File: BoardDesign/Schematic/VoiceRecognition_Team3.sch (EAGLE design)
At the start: 52 parts, among them J1 5.5x2.1mm Barrel, Q1 16MHz, X1 USB-A

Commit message: Added Updated Board and BOM, note this will not be the final revision
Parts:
- removed C6: 100nF, rcl:C-USC1206
- removed C7: 10uF, rcl:C-USC1206
- removed LED_GRN, LED_RED, LED_YLW, PWR-BLU: (no value), led:LEDSMT1206
- removed MIC_ON: (no value), adafruit:SWITCH_PUSHBUTTONC&K_KSS
- added LEDARRAY: (no value), adafruit:PINHD-1X8BIG
- added LOCK_RESET: (no value), adafruit:PINHD-1X3
- renumbered JP1 to ICSP_INPUT, JP2 to MIC_INPUT, JP3 to SERVO_OUT
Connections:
- net N$13 renamed MOSI
- net N$17 renamed MISO
- net N$2 renamed SCK
- removed net N$15: C7.1, MIC_INPUT.2, MIC_ON.P$2, VCC_TO_MIC.TP
- removed net N$8: LED_RED.C, R3.2
- removed net SERVO_POS: J1.PWR, SERVO_OUT.1, V_BARREL.TP
- new net LOCK_RESET: LOCK_RESET.2, U$1.PB7(OC0A/OC1C/RTS)
- new net N$2: USB_TO_GND.TP, X1.GND
- new net N$4: LEDARRAY.1, R6.1
- net FUNC_GRN: now also LEDARRAY.3, R7.1, R7.2; no longer LED_GRN.A
- net GND: now also LEDARRAY.2, LEDARRAY.4, LEDARRAY.6, LEDARRAY.8, LOCK_RESET.1; no longer C6.2, C7.2, R3.1, R5.1, R6.1, R7.1, USB_TO_GND.TP, X1.GND
- net N$5: now also LEDARRAY.5, R5.2; no longer PWR-BLU.C, R6.2
- net N$6: now also LEDARRAY.7, NOFUNC_RED.TP, R3.2; no longer LED_GRN.C, R7.2
- net N$7: now also VCC_TO_USB.TP, X1.VBUS; no longer LED_YLW.C, R5.2
- net NOFUNC_RED: now also R3.1; no longer LED_RED.A, NOFUNC_RED.TP
- net VCC: now also J1.PWR, MIC_INPUT.2, R6.2, SERVO_OUT.1, VCC_TO_MIC.TP, V_BARREL.TP; no longer C6.1, MIC_ON.P$1, PWR-BLU.A, VCC_TO_USB.TP, X1.VBUS
- net WARN_YELL: now also R5.1; no longer LED_YLW.A
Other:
- note added: "NC"
- note added: "Tactile Inputs"
- note removed: "PWR_BLU"
- note removed: "Reset Button"
- note removed: "WARN_YELL"
- moved on the sheet: FUNC_GRN, NOFUNC_RED, PWR_BLU, R3, R5, R6, R7, VCC_TO_MIC, WARN_YELL

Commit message: Added a few changes to the board per andrew's suggestion
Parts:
- added C10, C11, C6, C7, C9: 100nF, rcl:C-USC1206
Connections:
- net GND: now also C10.2, C11.2, C6.2, C7.2, C9.2
- net VCC: now also C10.1, C11.1, C6.1, C7.1, C9.1
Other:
- moved on the sheet: C1, C12, C2, Q1

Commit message: Added a connection to ground in the USB jack
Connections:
- removed net N$2: USB_TO_GND.TP, X1.GND
- net GND: now also USB_TO_GND.TP, X1.GND
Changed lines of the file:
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@@
 <part name="GND17" library="supply1" library_urn="urn:adsk.eagle:library:371" deviceset="GND" device=""/>
 <part name="GND21" library="supply1" library_urn="urn:adsk.eagle:library:371" deviceset="GND" device=""/>
+<part name="GND22" library="supply1" library_urn="urn:adsk.eagle:library:371" deviceset="GND" device=""/>
 </parts>
 <sheets>
@@
 <attribute name="VALUE" x="124.46" y="88.9" size="1.778" layer="96" rot="R270"/>
 </instance>
+<instance part="GND22" gate="1" x="33.02" y="88.9" smashed="yes">
+<attribute name="VALUE" x="30.48" y="86.36" size="1.778" layer="96"/>
+</instance>
 </instances>
 <busses>
@@
 <pinref part="C11" gate="G$1" pin="2"/>
 <pinref part="GND21" gate="1" pin="GND"/>
+</segment>
+<segment>
+<pinref part="X1" gate="G$1" pin="GND"/>
+<wire x1="33.02" y1="101.6" x2="33.02" y2="93.98" width="0.1524" layer="91"/>
+<pinref part="USB_TO_GND" gate="G$1" pin="TP"/>
+<pinref part="GND22" gate="1" pin="GND"/>
+<wire x1="33.02" y1="91.44" x2="33.02" y2="93.98" width="0.1524" layer="91"/>
+<junction x="33.02" y="93.98"/>
 </segment>
 </net>
@@
 </segment>
 </net>
-<net name="N$2" class="0">
-<segment>
-<pinref part="X1" gate="G$1" pin="GND"/>
-<wire x1="33.02" y1="101.6" x2="33.02" y2="93.98" width="0.1524" layer="91"/>
-<pinref part="USB_TO_GND" gate="G$1" pin="TP"/>
-</segment>
-</net>

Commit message: yeah
* rearranged bypass caps to VCC

* Added tolerances to bottom right of schem
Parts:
- renumbered VCC_TO_USB to TP_USB
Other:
- note added: "R1, R2, R3, R5, R6, R7: 250mW, 1% TOL"
- note removed: "250mW TOL: 1%"
- moved on the sheet: C10, C11, C12, C2, C6, C7, C9

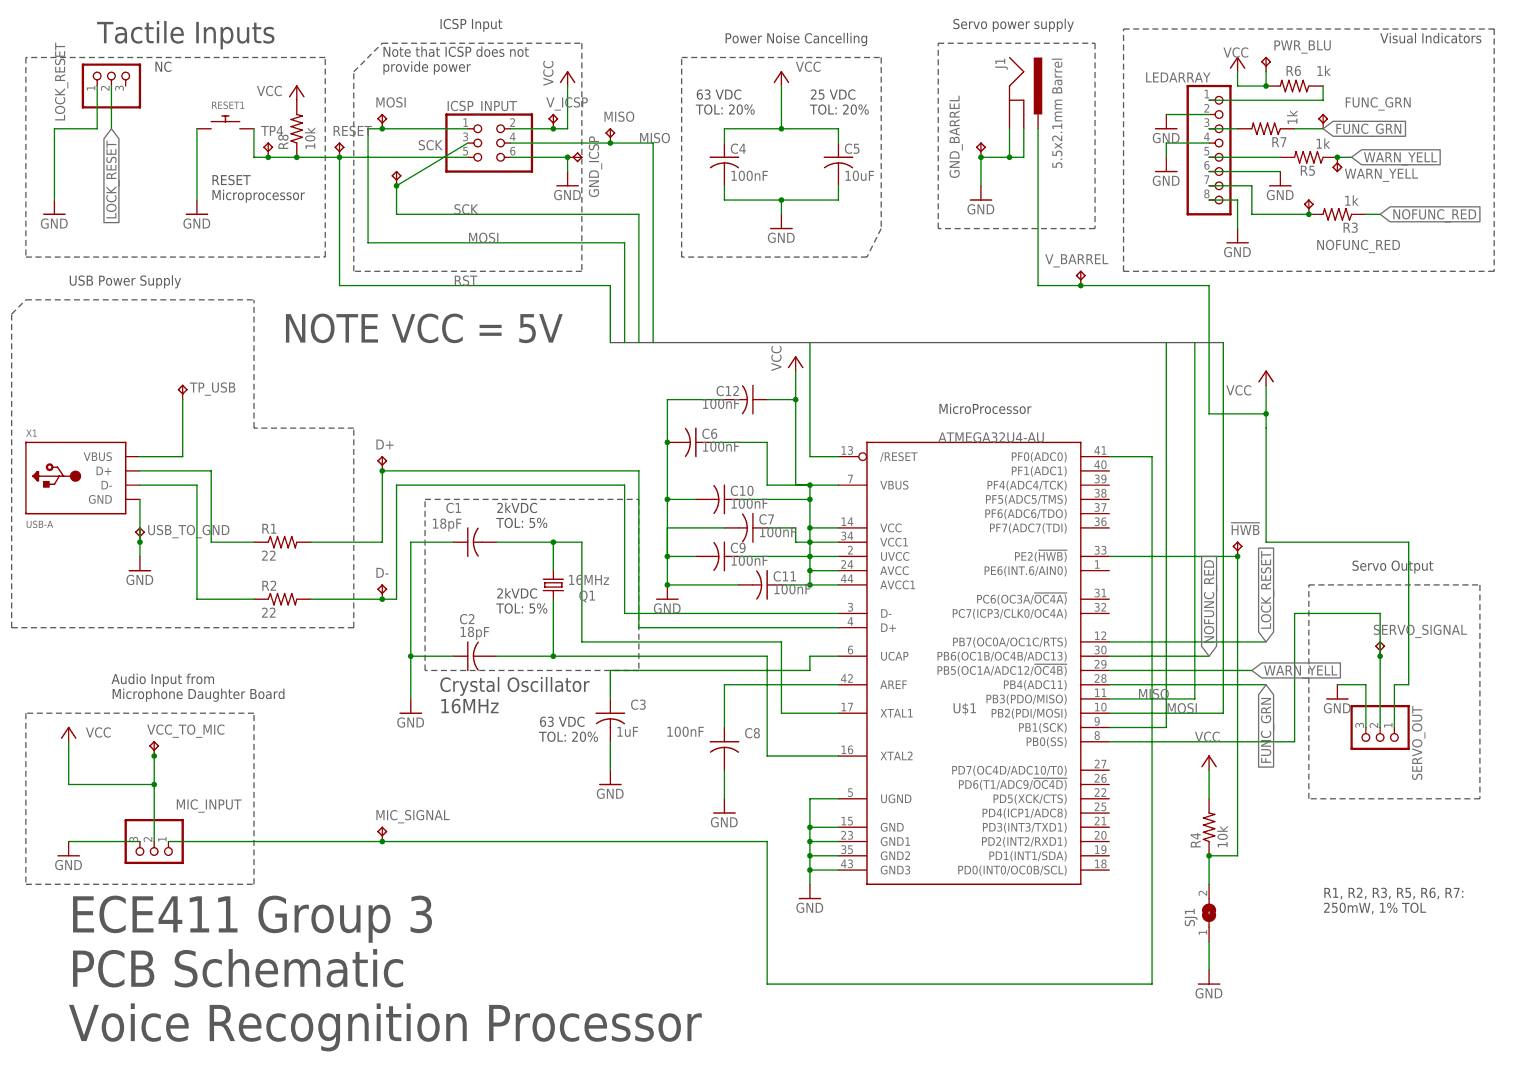
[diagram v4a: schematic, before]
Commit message: VCC caps + cosmetics
* Moved vcc bias caps onto board.
* Moved component names/values around for legibility.
* Rerouted some wires for cosmetic purposes.
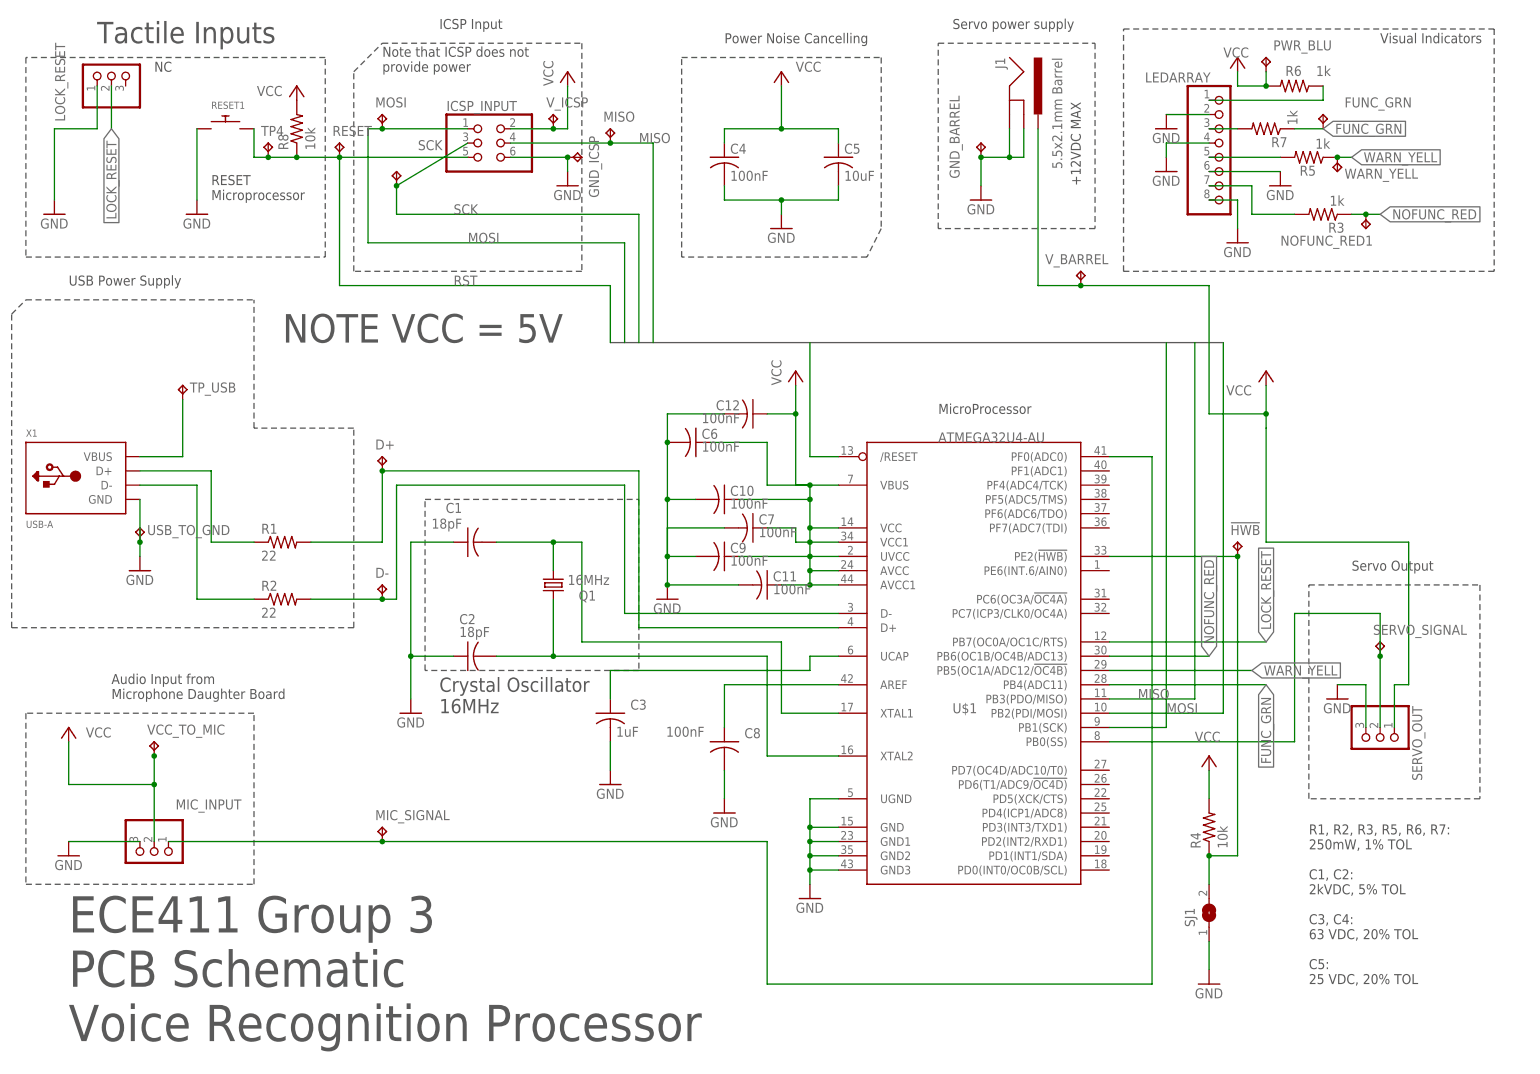
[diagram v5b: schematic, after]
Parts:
- removed NOFUNC_RED: TPTP15SQ, testpad:TPTP15SQ
- added NOFUNC_RED1: TPTP15SQ, testpad:TPTP15SQ
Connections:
- net N$6: no longer NOFUNC_RED.TP
- net NOFUNC_RED: now also NOFUNC_RED1.TP
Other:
- note added: "+12VDC MAX"
- note added: "R1, R2, R3, R5, R6, R7: 250mW, 1% TOL C1, C2: 2kVDC, 5% TOL C3, C4: 63 VDC, 20% TOL C5: 25 VDC, 20% TOL"
- note removed: "25 VDC TOL: 20%"
- note removed: "2kVDC TOL: 5%"
- note removed: "63 VDC TOL: 20%"
- note removed: "R1, R2, R3, R5, R6, R7: 250mW, 1% TOL"
- moved on the sheet: C12, R3
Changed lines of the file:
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@@
 </variantdefs>
 <classes>
-<class number="0" name="default" width="0" drill="0">
+<class number="0" name="VCC" width="0.05" drill="0">
+</class>
+<class number="1" name="GND" width="0.00126875" drill="0">
 </class>
 </classes>
@@
 <part name="FUNC_GRN" library="testpad" library_urn="urn:adsk.eagle:library:385" deviceset="TP" device="TP15SQ" package3d_urn="urn:adsk.eagle:package:27975/1"/>
 <part name="WARN_YELL" library="testpad" library_urn="urn:adsk.eagle:library:385" deviceset="TP" device="TP15SQ" package3d_urn="urn:adsk.eagle:package:27975/1"/>
-<part name="NOFUNC_RED" library="testpad" library_urn="urn:adsk.eagle:library:385" deviceset="TP" device="TP15SQ" package3d_urn="urn:adsk.eagle:package:27975/1"/>
 <part name="!HWB" library="testpad" library_urn="urn:adsk.eagle:library:385" deviceset="TP" device="TP15SQ" package3d_urn="urn:adsk.eagle:package:27975/1"/>
 <part name="RESET" library="testpad" library_urn="urn:adsk.eagle:library:385" deviceset="TP" device="TP15SQ" package3d_urn="urn:adsk.eagle:package:27975/1"/>
@@
 <part name="GND21" library="supply1" library_urn="urn:adsk.eagle:library:371" deviceset="GND" device=""/>
 <part name="GND22" library="supply1" library_urn="urn:adsk.eagle:library:371" deviceset="GND" device=""/>
+<part name="NOFUNC_RED1" library="testpad" library_urn="urn:adsk.eagle:library:385" deviceset="TP" device="TP15SQ" package3d_urn="urn:adsk.eagle:package:27975/1"/>
 </parts>
 <sheets>
@@
 <wire x1="241.3" y1="48.26" x2="241.3" y2="86.36" width="0.1524" layer="97" style="shortdash"/>
 <text x="248.92" y="88.9" size="1.778" layer="97">Servo Output</text>
-<text x="132.08" y="170.18" size="1.778" layer="97">63 VDC
-TOL: 20%</text>
-<text x="152.4" y="170.18" size="1.778" layer="97">25 VDC
-TOL: 20%</text>
-<text x="104.14" y="58.42" size="1.778" layer="97">63 VDC
-TOL: 20%</text>
-<text x="96.52" y="81.28" size="1.778" layer="97">2kVDC
-TOL: 5%</text>
-<text x="96.52" y="96.52" size="1.778" layer="97">2kVDC
-TOL: 5%</text>
 <text x="76.2" y="177.8" size="1.778" layer="97">Note that ICSP does not
 provide power</text>
@@
 <wire x1="208.28" y1="142.24" x2="208.28" y2="185.42" width="0.1524" layer="97" style="shortdash"/>
 <text x="35.56" y="177.8" size="1.778" layer="97">NC</text>
-<text x="243.84" y="27.94" size="1.778" layer="97">R1, R2, R3, R5, R6, R7:
-250mW, 1% TOL</text>
+<text x="241.3" y="15.24" size="1.778" layer="97">R1, R2, R3, R5, R6, R7:
+250mW, 1% TOL
+C1, C2:
+2kVDC, 5% TOL
+C3, C4:
+63 VDC, 20% TOL
+C5:
+25 VDC, 20% TOL</text>
+<text x="200.66" y="157.48" size="1.778" layer="97" rot="R90">+12VDC MAX</text>
 </plain>
 <instances>
@@
 <attribute name="VALUE" x="54.61" y="80.518" size="1.778" layer="96"/>
 </instance>
-<instance part="R3" gate="G$1" x="246.38" y="152.4" rot="R180">
-<attribute name="NAME" x="250.19" y="150.9014" size="1.778" layer="95" rot="R180"/>
-<attribute name="VALUE" x="250.19" y="155.702" size="1.778" layer="96" rot="R180"/>
+<instance part="R3" gate="G$1" x="243.84" y="152.4" rot="R180">
+<attribute name="NAME" x="247.65" y="150.9014" size="1.778" layer="95" rot="R180"/>
+<attribute name="VALUE" x="247.65" y="155.702" size="1.778" layer="96" rot="R180"/>
 </instance>
 <instance part="R4" gate="G$1" x="223.52" y="43.18" rot="R90">
@@
 <attribute name="VALUE" x="226.06" y="180.34" size="1.778" layer="96"/>
 </instance>
-<instance part="P+12" gate="VCC" x="149.86" y="127">
-<attribute name="VALUE" x="147.32" y="124.46" size="1.778" layer="96" rot="R90"/>
+<instance part="P+12" gate="VCC" x="149.86" y="124.46">
+<attribute name="VALUE" x="147.32" y="121.92" size="1.778" layer="96" rot="R90"/>
 </instance>
 <instance part="P+13" gate="VCC" x="223.52" y="55.88">
@@
 <attribute name="VALUE" x="58.42" y="175.26" size="1.778" layer="96" rot="R180"/>
 </instance>
-<instance part="C12" gate="G$1" x="142.24" y="119.38" rot="R270">
-<attribute name="NAME" x="135.636" y="120.015" size="1.778" layer="95"/>
-<attribute name="VALUE" x="133.096" y="117.729" size="1.778" layer="96"/>
+<instance part="C12" gate="G$1" x="142.24" y="116.84" rot="R270">
+<attribute name="NAME" x="135.636" y="117.475" size="1.778" layer="95"/>
+<attribute name="VALUE" x="133.096" y="115.189" size="1.778" layer="96"/>
 </instance>
 <instance part="J1" gate="G$1" x="185.42" y="170.18" rot="R270">
@@
 <attribute name="TP_SIGNAL_NAME" x="245.11" y="161.29" size="1.778" layer="97" rot="R180"/>
 </instance>
-<instance part="NOFUNC_RED" gate="G$1" x="241.3" y="154.94">
-<attribute name="NAME" x="242.57" y="146.05" size="1.778" layer="95"/>
-<attribute name="TP_SIGNAL_NAME" x="242.57" y="153.67" size="1.778" layer="97"/>
-</instance>
 <instance part="!HWB" gate="G$1" x="228.6" y="93.98">
 <attribute name="NAME" x="227.33" y="95.25" size="1.778" layer="95"/>
@@
 <instance part="GND22" gate="1" x="33.02" y="88.9">
 <attribute name="VALUE" x="30.48" y="86.36" size="1.778" layer="96"/>
+</instance>
+<instance part="NOFUNC_RED1" gate="G$1" x="251.46" y="149.86" rot="R180">
+<attribute name="NAME" x="252.73" y="148.59" size="1.778" layer="95" rot="R180"/>
+<attribute name="TP_SIGNAL_NAME" x="250.19" y="151.13" size="1.778" layer="97" rot="R180"/>
 </instance>
 </instances>
@@
 <junction x="127" y="101.6"/>
 <pinref part="C12" gate="G$1" pin="2"/>
-<wire x1="137.16" y1="119.38" x2="127" y2="119.38" width="0.1524" layer="91"/>
-<wire x1="127" y1="119.38" x2="127" y2="111.76" width="0.1524" layer="91"/>
+<wire x1="137.16" y1="116.84" x2="127" y2="116.84" width="0.1524" layer="91"/>
+<wire x1="127" y1="116.84" x2="127" y2="111.76" width="0.1524" layer="91"/>
 <junction x="127" y="111.76"/>
 </segment>
@@
 <segment>
 <pinref part="R3" gate="G$1" pin="1"/>
+<wire x1="248.92" y1="152.4" x2="251.46" y2="152.4" width="0.1524" layer="91"/>
+<label x="254" y="152.4" size="1.778" layer="95" xref="yes"/>
+<pinref part="NOFUNC_RED1" gate="G$1" pin="TP"/>
 <wire x1="251.46" y1="152.4" x2="254" y2="152.4" width="0.1524" layer="91"/>
-<label x="254" y="152.4" size="1.778" layer="95" xref="yes"/>
+<junction x="251.46" y="152.4"/>
 </segment>
 </net>
@@
 <pinref part="P+12" gate="VCC" pin="VCC"/>
 <pinref part="U$1" gate="G$1" pin="VBUS"/>
-<wire x1="149.86" y1="124.46" x2="149.86" y2="119.38" width="0.1524" layer="91"/>
-<wire x1="149.86" y1="119.38" x2="149.86" y2="104.14" width="0.1524" layer="91"/>
+<wire x1="149.86" y1="121.92" x2="149.86" y2="116.84" width="0.1524" layer="91"/>
+<wire x1="149.86" y1="116.84" x2="149.86" y2="104.14" width="0.1524" layer="91"/>
 <wire x1="149.86" y1="104.14" x2="152.4" y2="104.14" width="0.1524" layer="91"/>
 <pinref part="U$1" gate="G$1" pin="VCC"/>
@@
 <wire x1="144.78" y1="111.76" x2="144.78" y2="104.14" width="0.1524" layer="91"/>
 <pinref part="C12" gate="G$1" pin="1"/>
-<wire x1="144.78" y1="119.38" x2="149.86" y2="119.38" width="0.1524" layer="91"/>
-<junction x="149.86" y="119.38"/>
+<wire x1="144.78" y1="116.84" x2="149.86" y2="116.84" width="0.1524" layer="91"/>
+<junction x="149.86" y="116.84"/>
 </segment>
 <segment>
@@
 <wire x1="223.52" y1="157.48" x2="231.14" y2="157.48" width="0.1524" layer="91"/>
 <wire x1="231.14" y1="157.48" x2="231.14" y2="152.4" width="0.1524" layer="91"/>
-<wire x1="231.14" y1="152.4" x2="241.3" y2="152.4" width="0.1524" layer="91"/>
-<pinref part="NOFUNC_RED" gate="G$1" pin="TP"/>
+<wire x1="231.14" y1="152.4" x2="238.76" y2="152.4" width="0.1524" layer="91"/>
 <pinref part="R3" gate="G$1" pin="2"/>
-<junction x="241.3" y="152.4"/>
-</segment>
-</net>
+</segment>
+</net>
